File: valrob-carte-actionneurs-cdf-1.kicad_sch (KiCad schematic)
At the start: 0 parts

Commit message: schem: import esp32s3 from valrob-pami
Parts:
- added AE1: Antenna, RF_Antenna:Johanson_2450AT18x100, symbol Device:Antenna
- added C18, C19: 1p2, Capacitor_SMD:C_0402_1005Metric, symbol Device:C
- added C20, C23, C27: 1u, Capacitor_SMD:C_0402_1005Metric, symbol Device:C
- added C21: 10u, Capacitor_SMD:C_0402_1005Metric, symbol Device:C
- added C22, C24, C25, C26: 0u1, Capacitor_SMD:C_0402_1005Metric, symbol Device:C
- added J10: Conn_01x04_Pin, Connector_PinHeader_2.54mm:PinHeader_1x04_P2.54mm_Vertical, symbol Connector:Conn_01x04_Pin
- added L3: 6n8, Inductor_SMD:L_0402_1005Metric, symbol Device:L
- added L4: L, Inductor_SMD:L_0402_1005Metric, symbol Device:L
- added L5, L6: 2n7, Inductor_SMD:L_0402_1005Metric, symbol Device:L
- added R21, R23: 10k, Resistor_SMD:R_0402_1005Metric, symbol Device:R
- added R22: 470, Resistor_SMD:R_0402_1005Metric, symbol Device:R
- added R24, R25: 22, Resistor_SMD:R_0402_1005Metric, symbol Device:R
- added R50: 0, Resistor_SMD:R_0402_1005Metric, symbol Device:R
- added U5: ESP32-S3FN8, Package_DFN_QFN:QFN-56-1EP_7x7mm_P0.4mm_EP4x4mm_ThermalVias, symbol PCM_Espressif:ESP32-S3
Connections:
- new net: L3.2, L4.1, R50.1
- new net: J10.4 (Pin_4), R22.1
- new net +3V3: C21.1, C22.1, C25.1, C26.1, C27.1, J10.1 (Pin_1), L6.1, R21.1, R23.2, U5.20 (VDD3P3_RTC), U5.46 (VDD3P3_CPU), U5.55 (VDDA), U5.56 (VDDA)
- new net BOOT: R23.1, U5.5 (GPIO0/BOOT)
- new net CHIP_PU: C20.1, R21.2, U5.4 (CHIP_PU/RESET)
- new net D+: R24.2
- new net D-: R25.2
- new net EMS: U5.8 (GPIO3/ADC1_CH2)
- new net ESP_D+: R24.1, U5.26 (GPIO20/USB_D+/ADC2_CH9)
- new net ESP_D-: R25.1, U5.25 (GPIO19/USB_D-/ADC2_CH8)
- new net GND: C18.2, C19.2, C20.2, C21.2, C22.2, C23.2, C24.2, C25.2, C26.2, C27.2, J10.3 (Pin_3), L4.2, U5.57 (GND)
- new net RF_ANT: AE1.1 (A), L3.1
- new net RF_ESP: C19.1, L5.2, U5.1 (LNA_IN/RF)
- new net RF_TRANS: C18.1, L5.1, R50.2
- new net U0RXD: J10.2 (Pin_2), U5.50 (U0RXD/PROG/GPIO44)
- new net U0TXD: R22.2, U5.49 (U0TXD/PROG/GPIO43)
- new net VDD3P3: C24.1, L6.2, U5.2 (VDD3P3), U5.3 (VDD3P3)
- new net VDD_SPI: C23.1, U5.29 (VDD_SPI)
- new net XTAL_N: U5.53 (XTAL_N)
- new net XTAL_P: U5.54 (XTAL_P)
- no-connect marks 0 -> 27
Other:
- note added: "EN RC delay"
- note added: "UART"

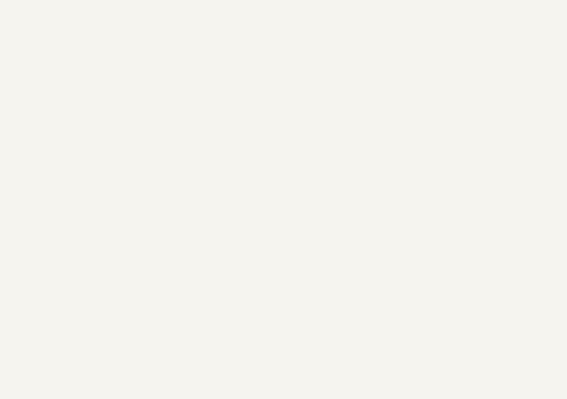
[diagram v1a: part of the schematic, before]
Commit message: schem: import esp32 HSE crystal
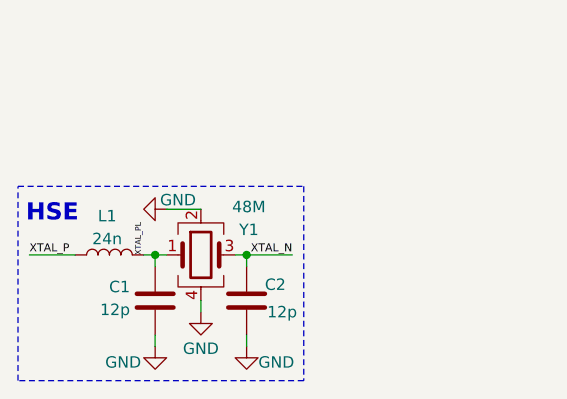
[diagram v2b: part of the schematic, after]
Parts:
- added C1, C2: 12p, Capacitor_SMD:C_0402_1005Metric, symbol Device:C
- added L1: 24n, Inductor_SMD:L_0402_1005Metric, symbol Device:L
- added Y1: 48M, Crystal:Crystal_SMD_2016-4Pin_2.0x1.6mm, symbol Device:Crystal_GND24
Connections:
- net GND: now also C1.1, C2.2, Y1.2, Y1.4
- net XTAL_N: now also C2.1, Y1.3
- net XTAL_P: now also L1.1
- new net XTAL_PL: C1.2, L1.2, Y1.1
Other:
- note added: "HSE"

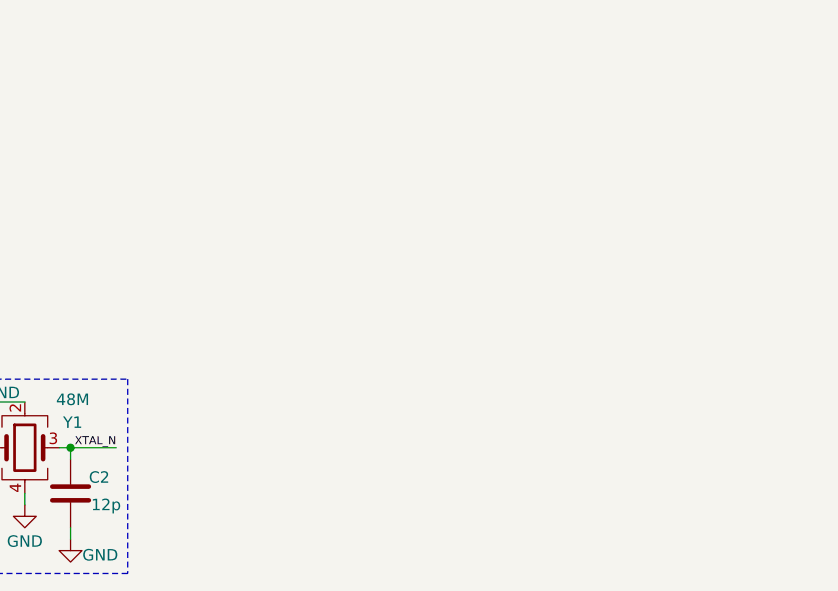
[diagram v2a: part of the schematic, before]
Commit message: schem: add USB c connector
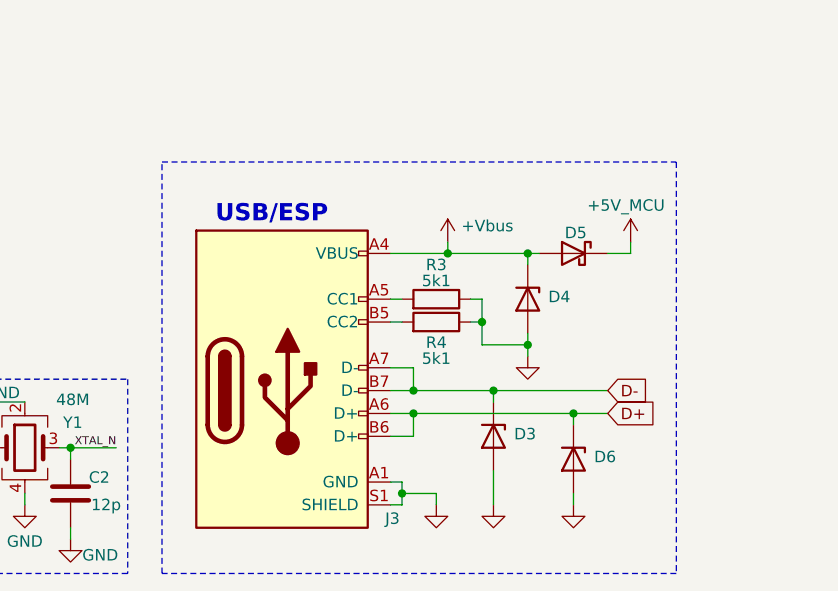
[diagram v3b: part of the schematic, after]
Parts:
- added D3, D4, D6: H5VU10U, GLCS:Diode_DFN1006, symbol GLCS:H5VU10U
- added D5: D_Schottky, Diode_SMD:D_SMA, symbol Device:D_Schottky
- added J3: USB_C_Receptacle_USB2.0_14P, Connector_USB:USB_C_Receptacle_HRO_TYPE-C-31-M-12, symbol Connector:USB_C_Receptacle_USB2.0_14P
- added R3, R4: 5k1, Resistor_SMD:R_0402_1005Metric, symbol Device:R
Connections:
- net D+: now also D6.1 (K), J3.A6 (D+), J3.B6 (D+)
- net D-: now also D3.1 (K), J3.A7 (D-), J3.B7 (D-)
- net GND: now also D3.2 (A), D4.2 (A), D6.2 (A), J3.A1 (GND), J3.A12 (GND), J3.B1 (GND), J3.B12 (GND), J3.S1 (SHIELD), R3.1, R4.1
- new net: J3.A5 (CC1), R3.2
- new net: J3.B5 (CC2), R4.2
- new net +5V_MCU: D5.1 (K)
- new net +Vbus: D4.1 (K), D5.2 (A), J3.A4 (VBUS), J3.A9 (VBUS), J3.B4 (VBUS), J3.B9 (VBUS)
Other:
- note added: "USB/ESP"

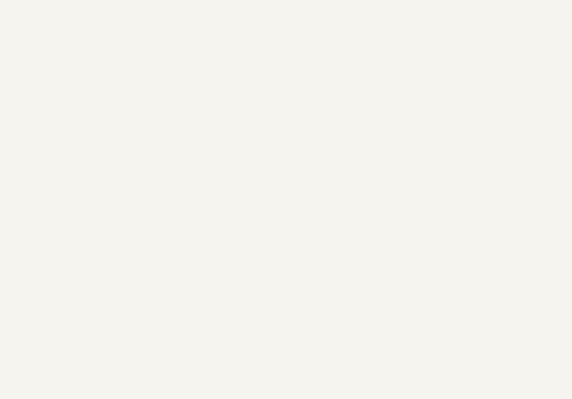
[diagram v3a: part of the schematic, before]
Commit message: schem: add servo connector
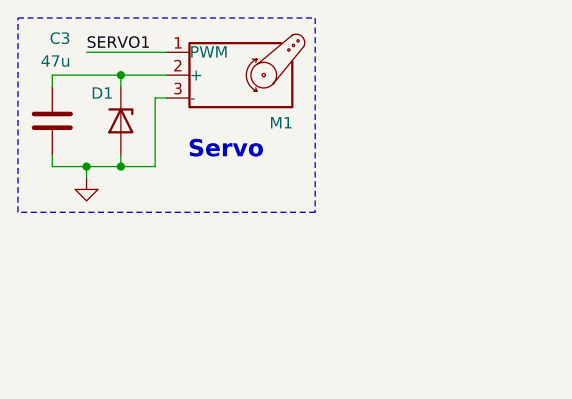
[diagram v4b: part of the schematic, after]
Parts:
- added C3: 47u, Capacitor_SMD:C_1206_3216Metric, symbol Device:C
- added D1: H5VU10U, GLCS:Diode_DFN1006, symbol GLCS:H5VU10U
- added M1: Motor_Servo, Connector_PinHeader_2.54mm:PinHeader_1x03_P2.54mm_Vertical, symbol Motor:Motor_Servo
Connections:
- net GND: now also C3.2, D1.2 (A), M1.3 (-)
- new net: C3.1, D1.1 (K), M1.2 (+)
- new net SERVO1: M1.1 (PWM)
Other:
- note added: "Servo"

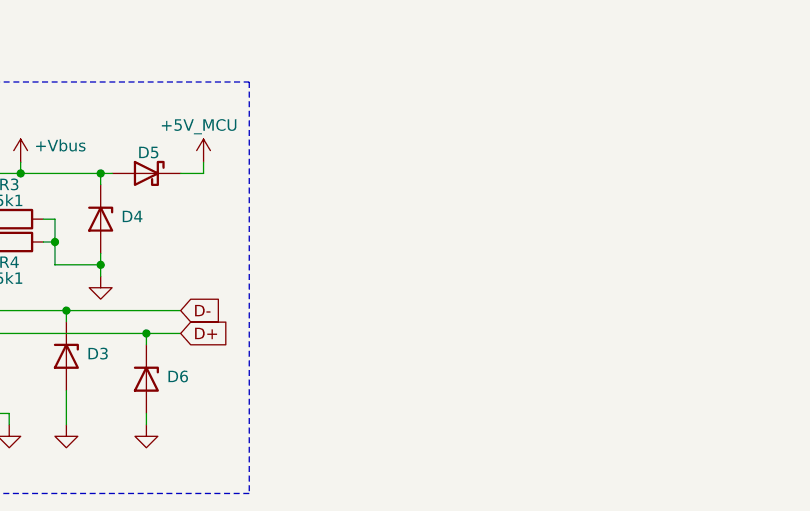
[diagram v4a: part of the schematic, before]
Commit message: schem: add led indicators
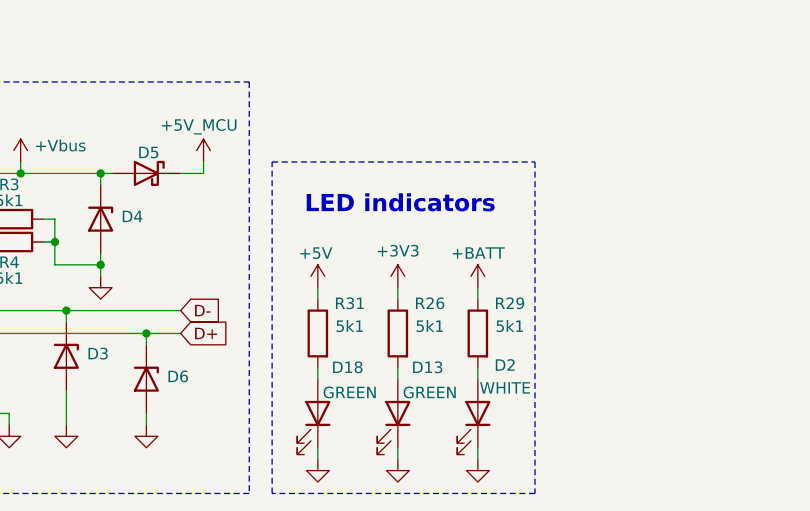
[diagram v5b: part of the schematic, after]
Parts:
- added D13, D18: GREEN, LED_SMD:LED_0805_2012Metric, symbol Device:LED
- added D2: WHITE, LED_SMD:LED_0603_1608Metric, symbol Device:LED
- added R26, R29, R31: 5k1, Resistor_SMD:R_0402_1005Metric, symbol Device:R
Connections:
- net +3V3: now also R26.1
- net GND: now also D13.1 (K), D18.1 (K), D2.1 (K)
- new net: D13.2 (A), R26.2
- new net: D18.2 (A), R31.2
- new net: D2.2 (A), R29.2
- new net +5V: R31.1
- new net +BATT: R29.1
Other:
- note added: "LED indicators"

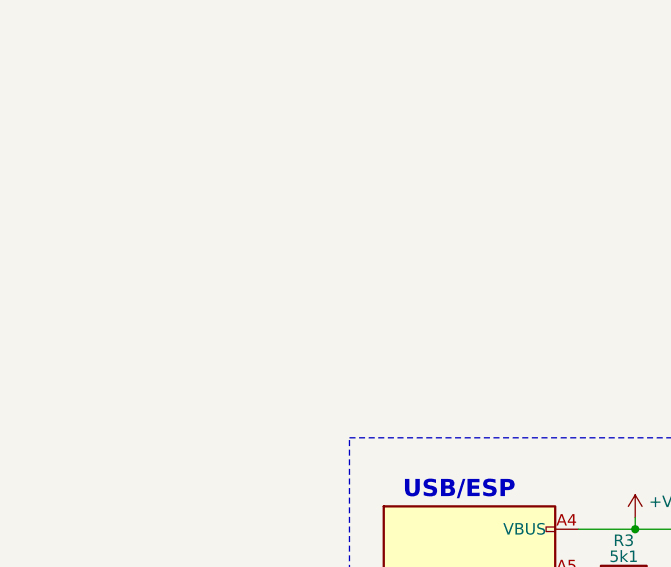
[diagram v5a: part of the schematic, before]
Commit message: schem: import LDL212 3V3 ldo
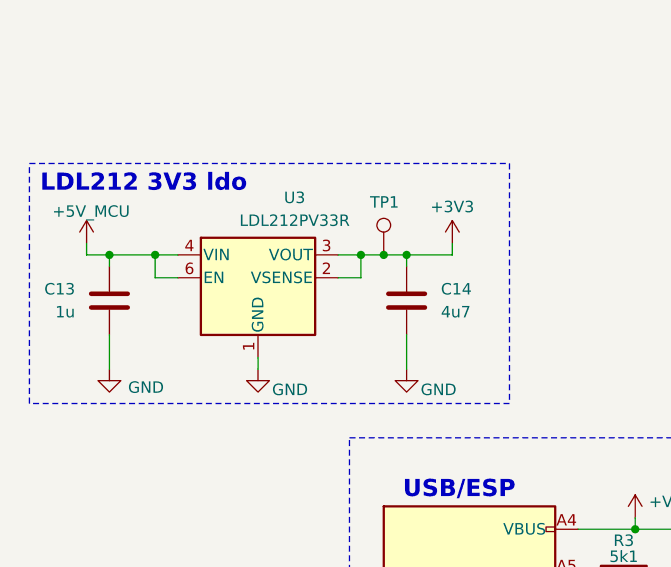
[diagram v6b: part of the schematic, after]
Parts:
- added C13: 1u, Capacitor_SMD:C_0402_1005Metric, symbol Device:C
- added C14: 4u7, Capacitor_SMD:C_0402_1005Metric, symbol Device:C
- added TP1: TestPoint, TestPoint:TestPoint_Pad_D2.0mm, symbol Connector:TestPoint
- added U3: LDL212PV33R, GLCS:DFN-6-1EP_2x2mm_P0.5mm_ST, symbol GLCS:LDL212PV33R
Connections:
- net +3V3: now also C14.1, TP1.1, U3.2 (VSENSE), U3.3 (VOUT)
- net +5V_MCU: now also C13.1, U3.4 (VIN), U3.6 (EN)
- net GND: now also C13.2, C14.2, U3.1 (GND)
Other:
- note added: "LDL212 3V3 ldo"

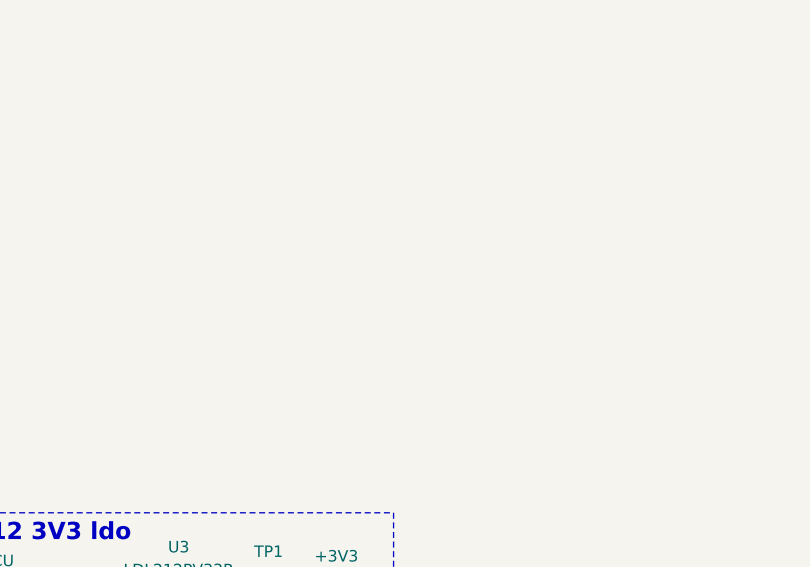
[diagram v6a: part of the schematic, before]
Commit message: schem: add TPS259472A 5v power input efuse
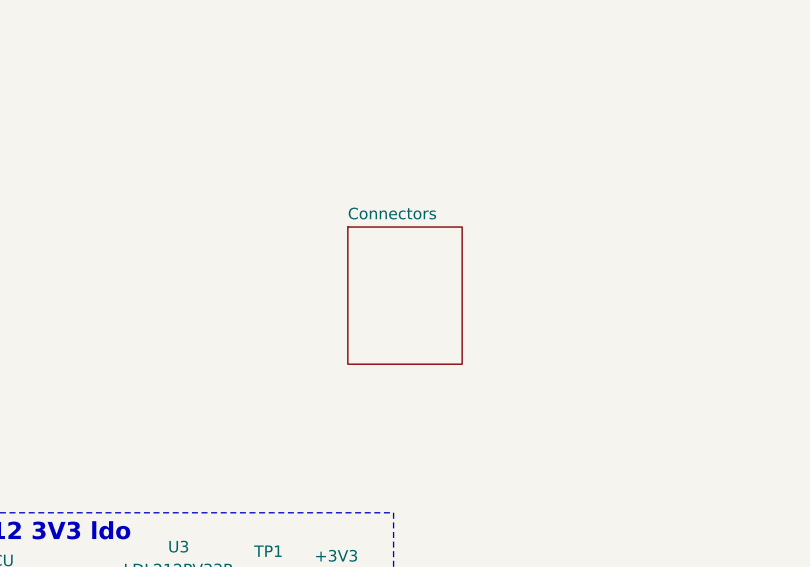
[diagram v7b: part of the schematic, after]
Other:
- added sheet Connectors (connectors.kicad_sch)
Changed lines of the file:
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@@
+		)
+	)
+	(sheet
+		(at 63.5 87.63)
+		(size 12.7 15.24)
+		(exclude_from_sim no)
+		(in_bom yes)
+		(on_board yes)
+		(dnp no)
+		(fields_autoplaced yes)
+		(stroke
+			(width 0.1524)
+			(type solid)
+		)
+		(fill
+			(color 0 0 0 0.0000)
+		)
+		(property "Sheetname" "Connectors"
+			(at 63.5 86.9184 0)
+			(effects
+				(font
+					(size 1.27 1.27)
+				)
+				(justify left bottom)
+			)
+		)
+		(property "Sheetfile" "connectors.kicad_sch"
+			(at 63.5 103.4546 0)
+			(effects
+				(font
+					(size 1.27 1.27)
+				)
+				(justify left top)
+				(hide yes)
+			)
+		)
+		(instances
+			(project "valrob-carte-actionneurs-cdf-1"
+				(path "/6d04427e-e45e-4b7f-8323-501f87acc543"
+					(page "2")
+				)
+			)
 		)
 	)

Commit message: schem: configure efuse
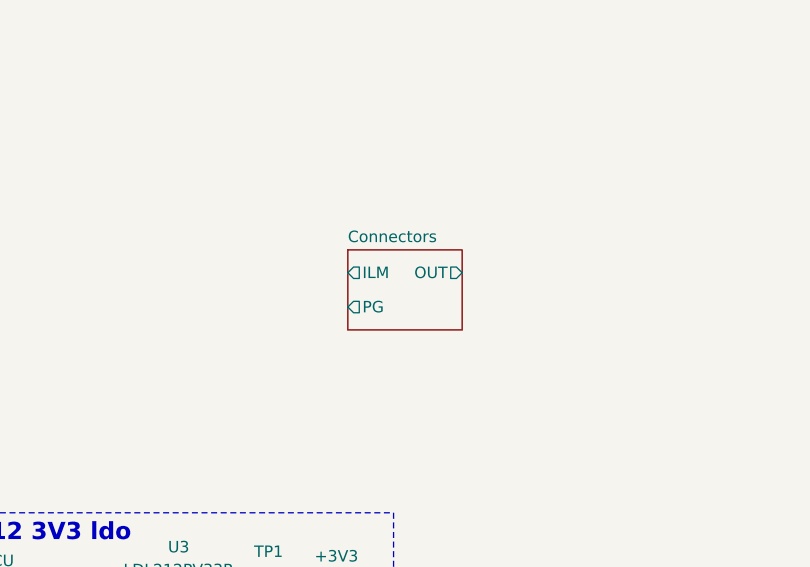
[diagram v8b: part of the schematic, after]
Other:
- sheet Connectors ports: added ILM, OUT, PG; removed none
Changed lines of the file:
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@@
 	)
 	(sheet
-		(at 63.5 87.63)
-		(size 12.7 15.24)
+		(at 63.5 90.17)
+		(size 12.7 8.89)
 		(exclude_from_sim no)
 		(in_bom yes)
@@
 		)
 		(property "Sheetname" "Connectors"
-			(at 63.5 86.9184 0)
+			(at 63.5 89.4584 0)
 			(effects
 				(font
@@
 		)
 		(property "Sheetfile" "connectors.kicad_sch"
-			(at 63.5 103.4546 0)
+			(at 63.5 99.6446 0)
 			(effects
 				(font
@@
 			)
 		)
+		(pin "ILM" output
+			(at 63.5 92.71 180)
+			(effects
+				(font
+					(size 1.27 1.27)
+				)
+				(justify left)
+			)
+		)
+		(pin "OUT" output
+			(at 76.2 92.71 0)
+			(effects
+				(font
+					(size 1.27 1.27)
+				)
+				(justify right)
+			)
+		)
+		(pin "PG" output
+			(at 63.5 96.52 180)
+			(effects
+				(font
+					(size 1.27 1.27)
+				)
+				(justify left)
+			)
+		)
